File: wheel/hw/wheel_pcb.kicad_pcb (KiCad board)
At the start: 2 copper layers, 36 x 67 mm, 48 parts, among them J2 DEBUG, J3 IO_C, J4 CAR, J5 IO_B, J6 IO_A, SW1 CONFIG, U1 LPC11C24FBD48, U2 TPS62175, U3 TLV70233_SOT23-5, Y1 12MHz

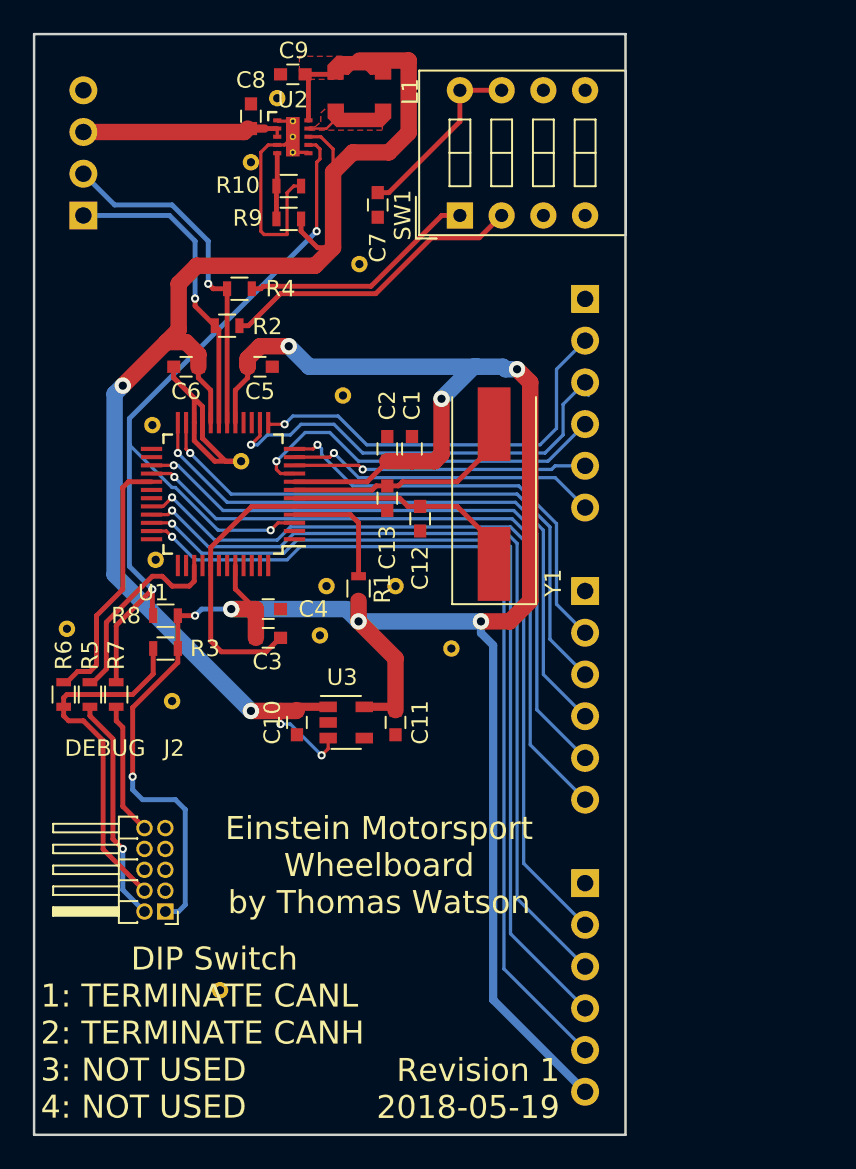
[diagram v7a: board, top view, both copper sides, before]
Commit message: add mounting holes to wheelboard
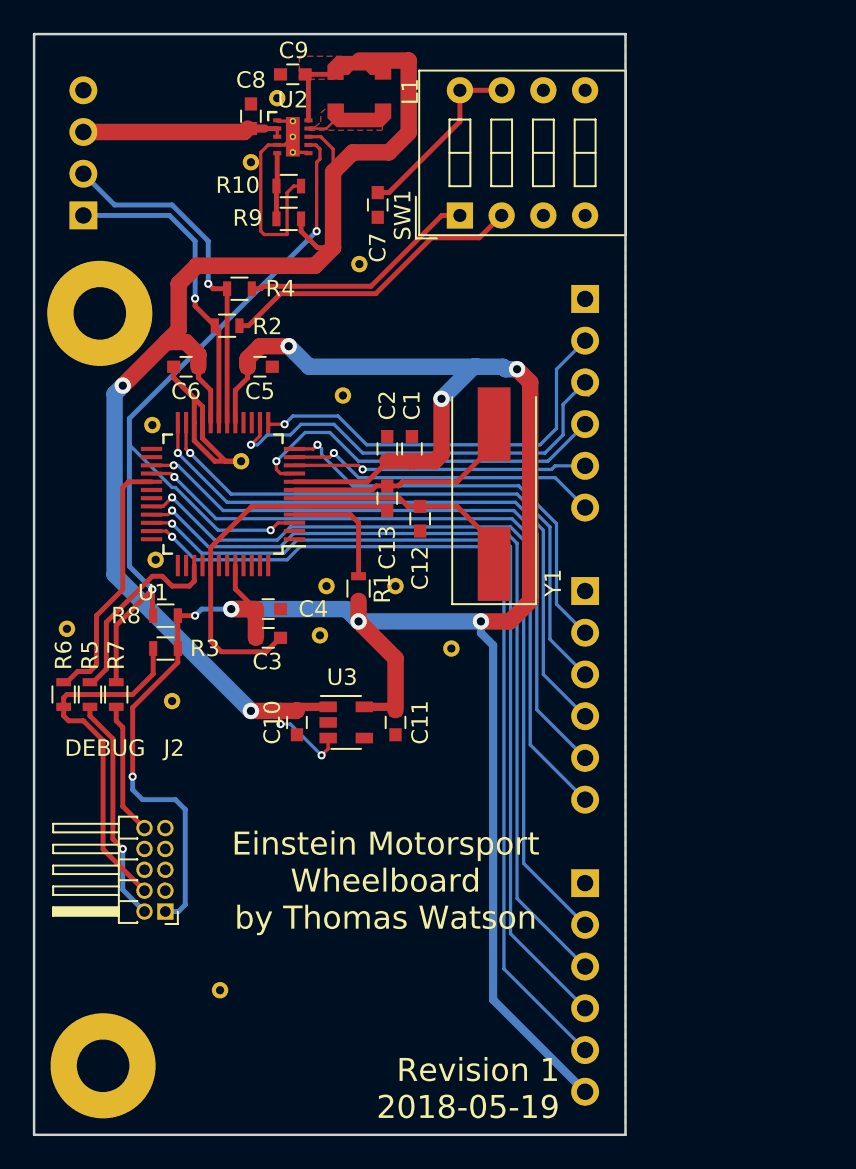
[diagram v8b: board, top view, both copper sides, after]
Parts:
- added REF**: MountingHole_3.2mm_M3, Mounting_Holes:MountingHole_3.2mm_M3_Pad, F.Cu at (227.2, 117.8)
- added REF**: MountingHole_3.2mm_M3, Mounting_Holes:MountingHole_3.2mm_M3_Pad, F.Cu at (227.0, 72.0)
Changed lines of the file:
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@@
 (kicad_pcb (version 4) (host pcbnew 4.0.7)
   (general
-    (links 118)
+    (links 120)
     (no_connects 0)
     (area 222.924999 54.924999 259.075001 122.075001)
@@
     (tracks 404)
     (zones 0)
-    (modules 48)
+    (modules 50)
     (nets 60)
   )
@@
   )
   (setup
-    (last_trace_width 1)
+    (last_trace_width 0.15)
     (user_trace_width 0.2)
     (user_trace_width 0.3)
@@
     (mod_text_size 1 1)
     (mod_text_width 0.15)
-    (pad_size 1 1)
-    (pad_drill 0.5)
+    (pad_size 6.4 6.4)
+    (pad_drill 3.2)
     (pad_to_mask_clearance 0.2)
     (aux_axis_origin 0 0)
     (visible_elements FFFFFF7F)
     (pcbplotparams
-      (layerselection 0x00030_80000001)
+      (layerselection 0x010f0_80000001)
       (usegerberextensions false)
       (excludeedgelayer true)
@@
       (plotinvisibletext false)
       (padsonsilk false)
-      (subtractmaskfromsilk false)
+      (subtractmaskfromsilk true)
       (outputformat 1)
       (mirror false)
-      (drillshape 1)
+      (drillshape 0)
       (scaleselection 1)
       (outputdirectory ""))
@@
     (add_net "Net-(U1-Pad48)")
   )
+  (module Mounting_Holes:MountingHole_3.2mm_M3_Pad locked (layer F.Cu)
+    (at 227.2 117.8)
+    (descr "Mounting Hole 3.2mm, M3")
+    (tags "mounting hole 3.2mm m3")
+    (zone_connect 2)
+    (attr virtual)
+    (fp_text reference REF** (at 0 -4.2) (layer F.SilkS) hide
+      (effects (font (size 1 1) (thickness 0.15)))
+    )
+    (fp_text value MountingHole_3.2mm_M3 (at 0 4.2) (layer F.Fab)
+      (effects (font (size 1 1) (thickness 0.15)))
+    )
+    (fp_text user %R (at 0.3 0) (layer F.Fab)
+      (effects (font (size 1 1) (thickness 0.15)))
+    )
+    (fp_circle (center 0 0) (end 3.2 0) (layer Cmts.User) (width 0.15))
+    (fp_circle (center 0 0) (end 3.45 0) (layer F.CrtYd) (width 0.05))
+    (pad 1 thru_hole circle (at 0 0) (size 6.4 6.4) (drill 3.2) (layers *.Cu *.Mask)
+      (net 1 GND) (zone_connect 2))
+  )
   (module custom_footprints:a_via locked (layer B.Cu)
     (at 225 91.2)
@@
     )
   )
+  (module Mounting_Holes:MountingHole_3.2mm_M3_Pad locked (layer F.Cu)
+    (at 227 72)
+    (descr "Mounting Hole 3.2mm, M3")
+    (tags "mounting hole 3.2mm m3")
+    (zone_connect 2)
+    (attr virtual)
+    (fp_text reference REF** (at 0 -4.2) (layer F.SilkS) hide
+      (effects (font (size 1 1) (thickness 0.15)))
+    )
+    (fp_text value MountingHole_3.2mm_M3 (at 0 4.2) (layer F.Fab)
+      (effects (font (size 1 1) (thickness 0.15)))
+    )
+    (fp_text user %R (at 0.3 0) (layer F.Fab)
+      (effects (font (size 1 1) (thickness 0.15)))
+    )
+    (fp_circle (center 0 0) (end 3.2 0) (layer Cmts.User) (width 0.15))
+    (fp_circle (center 0 0) (end 3.45 0) (layer F.CrtYd) (width 0.05))
+    (pad 1 thru_hole circle (at 0 0) (size 6.4 6.4) (drill 3.2) (layers *.Cu *.Mask)
+      (net 1 GND) (zone_connect 2))
+  )
   (gr_text "1:GND\n2:A1\n3:A2\n4:A3\n5:A4\n6:3.3V" (at 245.2 113) (layer B.SilkS)
     (effects (font (size 1.5 1.5) (thickness 0.3)) (justify left mirror))
@@
     (effects (font (size 1.4 1.4) (thickness 0.28)) (justify right))
   )
-  (gr_text "Einstein Motorsport\nWheelboard\nby Thomas Watson" (at 244 105.6) (layer F.SilkS)
+  (gr_text "Einstein Motorsport\nWheelboard\nby Thomas Watson" (at 244.4 106.55) (layer F.SilkS)
     (effects (font (size 1.4 1.4) (thickness 0.28)))
   )
-  (gr_text "         DIP Switch\n1: TERMINATE CANL\n2: TERMINATE CANH\n3: NOT USED\n4: NOT USED" (at 223.4 115.8) (layer F.SilkS)
-    (effects (font (size 1.4 1.4) (thickness 0.28)) (justify left))
+  (gr_text "DIP Switch\n1: TERMINATE CANL\n2: TERMINATE CANH\n3: NOT USED\n4: NOT USED" (at 230.35 78.05 90) (layer B.SilkS)
+    (effects (font (size 1.4 1.4) (thickness 0.28)) (justify left mirror))
   )
   (gr_line (start 259 122) (end 259 55) (layer Edge.Cuts) (width 0.15))
